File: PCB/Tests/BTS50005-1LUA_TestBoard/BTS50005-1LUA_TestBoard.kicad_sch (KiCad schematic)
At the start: 0 parts

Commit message: BTS50005-1LUA Evaluation board
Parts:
- added C1, C2: 10nF, Capacitor_SMD:C_0402_1005Metric, symbol Device:C_Small
- added C3: 100nF, Capacitor_SMD:C_0805_2012Metric, symbol Device:C_Small
- added D1: BAT54SW, Package_TO_SOT_SMD:SOT-323_SC-70, symbol Diode:BAT54SW
- added H1, H2: MountingHole_Pad, MountingHole:MountingHole_6.5mm_Pad_Via, symbol Mechanical:MountingHole_Pad
- added J1: Conn_01x06, Connector_Molex:Molex_Micro-Latch_53253-0670_1x06_P2.00mm_Vertical, symbol Connector_Generic:Conn_01x06
- added Q1: BTS500101LUAAUMA1, PDM_Additional:BTS500101LUAAUMA1, symbol BTS500101LUAAUMA1:BTS500101LUAAUMA1
- added R1, R3: 4.7k, Resistor_SMD:R_0402_1005Metric, symbol Device:R_Small
- added R2: 1k, Resistor_SMD:R_0402_1005Metric, symbol Device:R_Small
- added TP1: IN_TP, TestPoint:TestPoint_Keystone_5000-5004_Miniature, symbol Connector:TestPoint_Flag
- added TP2: OUT_TP, TestPoint:TestPoint_Keystone_5000-5004_Miniature, symbol Connector:TestPoint_Flag
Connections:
- new net +12V: C3.1, H1.1, Q1.9 (VS)
- new net CONTOLLER_VDD: D1.2, J1.6 (Pin_6)
- new net CONTROLER_DEN: J1.4 (Pin_4), R3.2
- new net CONTROLER_IN: J1.5 (Pin_5), R1.2, TP1.1
- new net CONTROLLER_ADC: C1.2, D1.3, J1.2 (Pin_2), Q1.2 (IS), R2.2
- new net DEN: Q1.4 (DEN), R3.1
- new net GND: C1.1, C2.1, C3.2, D1.1, J1.1 (Pin_1), Q1.1 (GND_), R2.1
- new net IN: Q1.3 (IN), R1.1
- new net OUT: C2.2, H2.1, Q1.5 (OUT), TP2.1
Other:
- note added: "BTS50010/05-1LUA Evaluation board"
- note added: "Sense resistor accuracy important!"

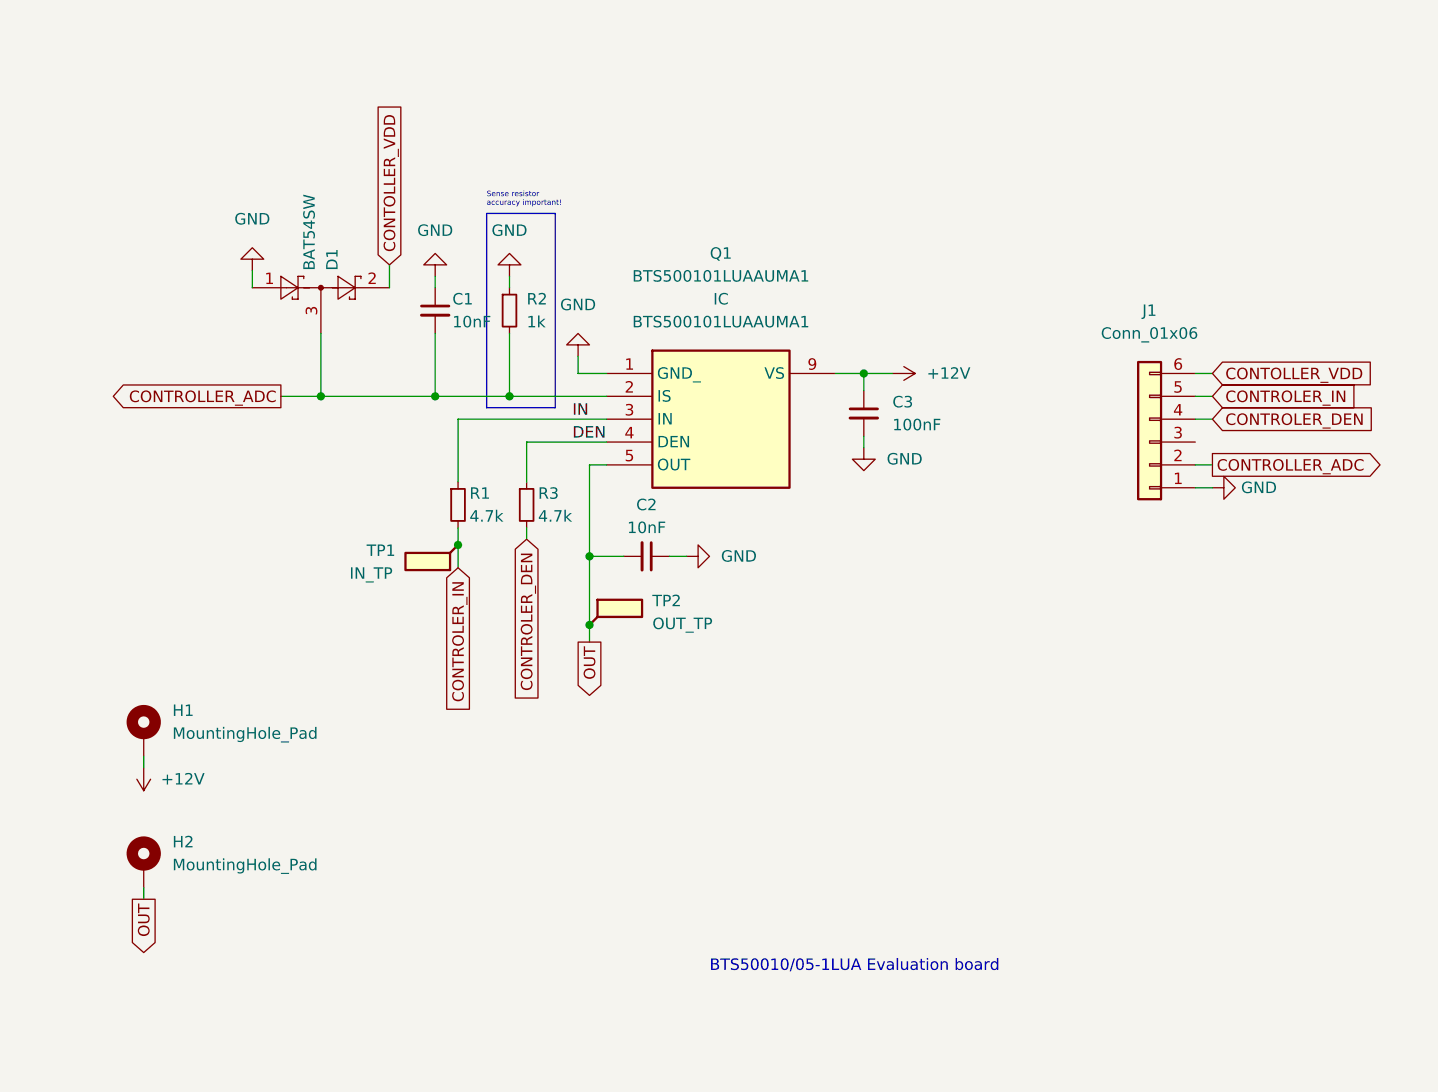
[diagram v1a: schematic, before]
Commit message: Added NTC for evaluation board
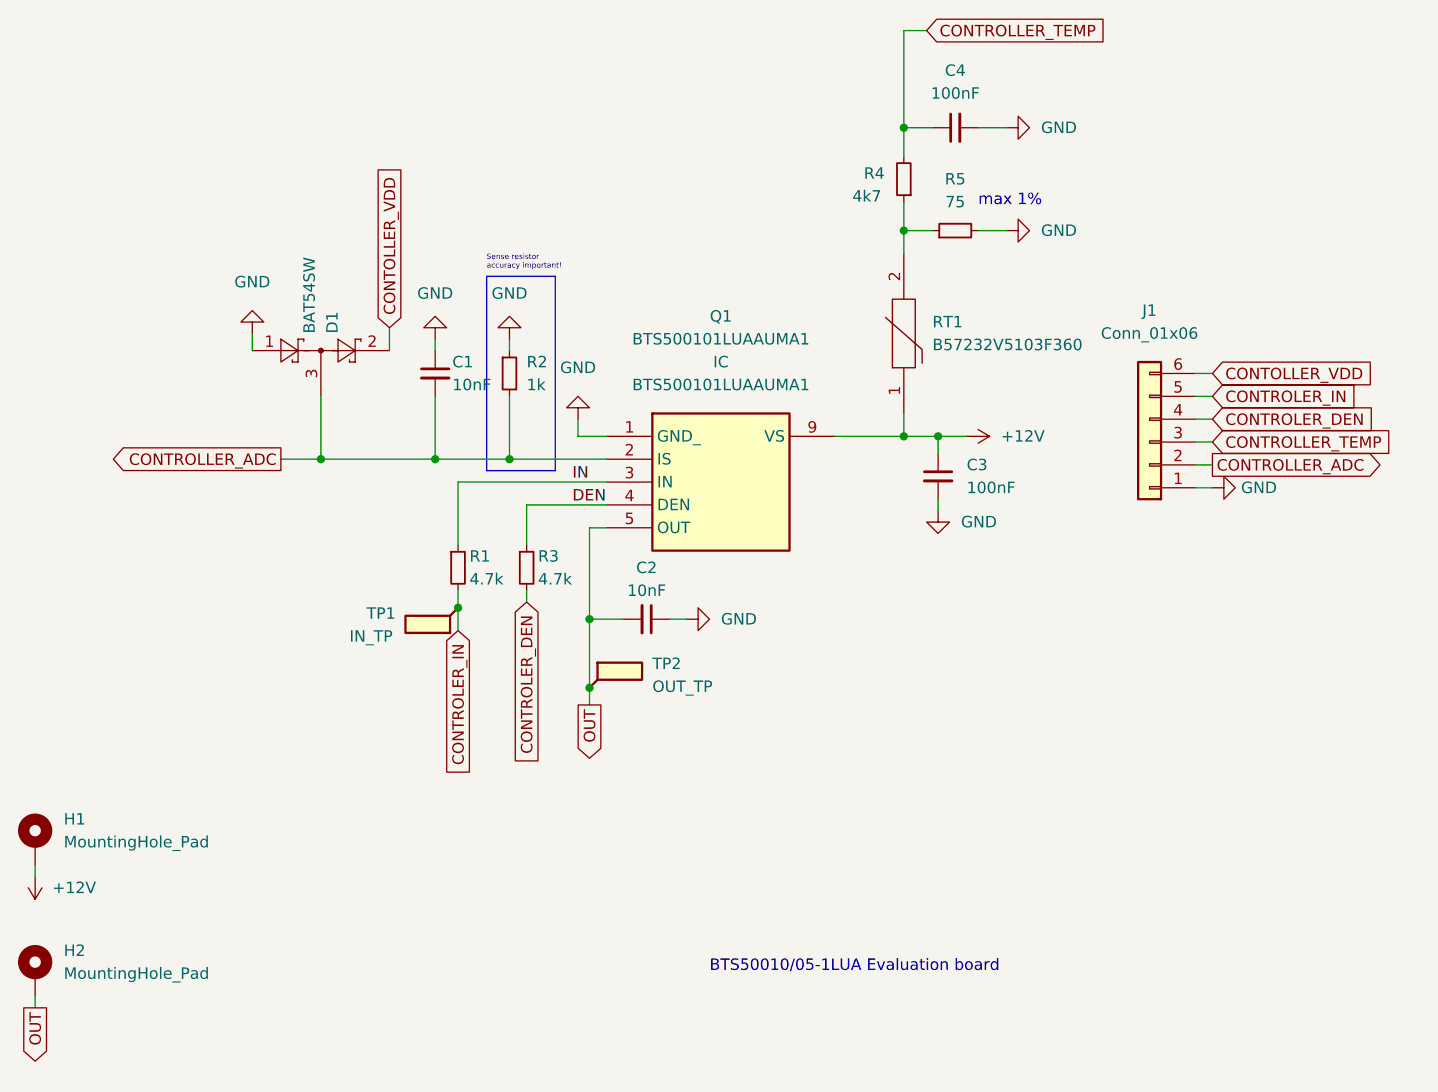
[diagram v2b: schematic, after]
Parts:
- added C4: 100nF, Capacitor_SMD:C_0402_1005Metric, symbol Device:C_Small
- added R4: 4k7, Resistor_SMD:R_0402_1005Metric, symbol Device:R_Small
- added R5: 75, Resistor_SMD:R_0402_1005Metric, symbol Device:R_Small
- added RT1: B57232V5103F360, PDM_Additional:THRMC1005X60N, symbol PDM_additional:B57232V5103F360
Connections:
- net +12V: now also RT1.1
- net GND: now also C4.2, R5.2
- net CONTROLLER_TEMP: now reaches J1.3 (Pin_3)
- net CONTROLLER_TEMP: now also C4.1, R4.2
- new net: R4.1, R5.1, RT1.2
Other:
- note added: "max 1%"
- moved on the sheet: C1, C2, C3, D1, H1, H2, Q1, R1, R2, R3, TP1, TP2

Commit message: Major changes with new switch
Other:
- note added: "LACKING CURRENT LIMITING RESISTOR ON IS AND CAPACITOR"
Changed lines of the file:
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@@
     (stroke (width 0) (type default) (color 0 0 0 0))
+  )
+  (text "LACKING CURRENT LIMITING RESISTOR ON IS AND CAPACITOR"
+    (at 25.908 69.85 0)
+    (effects (font (size 1.27 1.27) (thickness 0.254) bold italic) (justify left bottom))
   )
   (text "BTS50010/05-1LUA Evaluation board" (at 101.6 121.92 0)
